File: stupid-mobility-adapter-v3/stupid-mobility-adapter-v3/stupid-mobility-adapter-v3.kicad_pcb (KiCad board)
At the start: 2 copper layers, 94.9 x 93.5 mm, 35 parts, among them J1 BTS7968-0, J2 Act0-FB, J3 BTS7968-1, J4 Act1-FB, J5 ESTOP_INPUT, J6 UART, J7 Relays, J8 I2C, J9 BATT_MON_SELECT, Q1 2N3904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

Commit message: Added buzzer and servo input to v3 pcb
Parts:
- added BZ1: Buzzer, stuipid-electronics-components:Buzzer_ABT-460-RC, F.Cu at (225.6, 99.8)
- added J10: UART, Connector_PinHeader_2.54mm:PinHeader_1x02_P2.54mm_Vertical, F.Cu at (213.9, 92.7)
- added R14: 100, Resistor_THT:R_Axial_DIN0207_L6.3mm_D2.5mm_P7.62mm_Horizontal, F.Cu at (220.7, 97.5)
- moved J7 53.9 mm to (235.2, 90.7), turned to 0 degrees
- moved U3 12.1 mm to (249.5, 98.0)
- moved R3 11.7 mm to (172.7, 92.7), turned to 180 degrees
- moved J6 5.59 mm to (188.7, 96.0)
- moved J8 5.59 mm to (188.7, 88.4)
- moved U1 5.39 mm to (193.5, 84.1)
- moved R5 4.13 mm to (165.1, 89.4), turned to 0 degrees
- moved J9 1.26 mm to (165.1, 85.6)
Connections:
- U5 pad 30: unconnected-(U5-Pad30) -> /px_steer
- U5 pad 31: unconnected-(U5-Pad31) -> /px_throttle
- U5 pad 32: unconnected-(U5-Pad32) -> Net-(R14-Pad2)
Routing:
- net /px_steer: track 0.00 -> 24.5 mm
- net /px_throttle: track 0.00 -> 20.8 mm
- net Net-(J7-Pad3): track 17.7 -> 35.2 mm
- net Net-(R14-Pad2): track 0.00 -> 15.4 mm
- net /BDI: track 100.7 -> 114.6 mm
- net Net-(J7-Pad2): track 23.4 -> 35.7 mm
- net /KEY_SW: track 52.7 -> 63.8 mm
- net /REV: track 50.2 -> 56.2 mm
- net Net-(BZ1-Pad1): track 0.00 -> 5.80 mm
- net /RX: track 10.9 -> 16.5 mm
- net /TX: track 7.26 -> 13.0 mm
- net Net-(F1-Pad2): track 14.1 -> 19.2 mm
- net /SCL: track 27.7 -> 31.3 mm
- net /BATT_MON: track 67.7 -> 70.8 mm
- net Net-(R7-Pad1): track 30.9 -> 33.8 mm
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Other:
- board text added: "RX"
- board text added: "SCL"
- board text added: "SDA"
- board text added: "TX"
- board text added: "px4_steer"
- board text added: "px4_throttle"

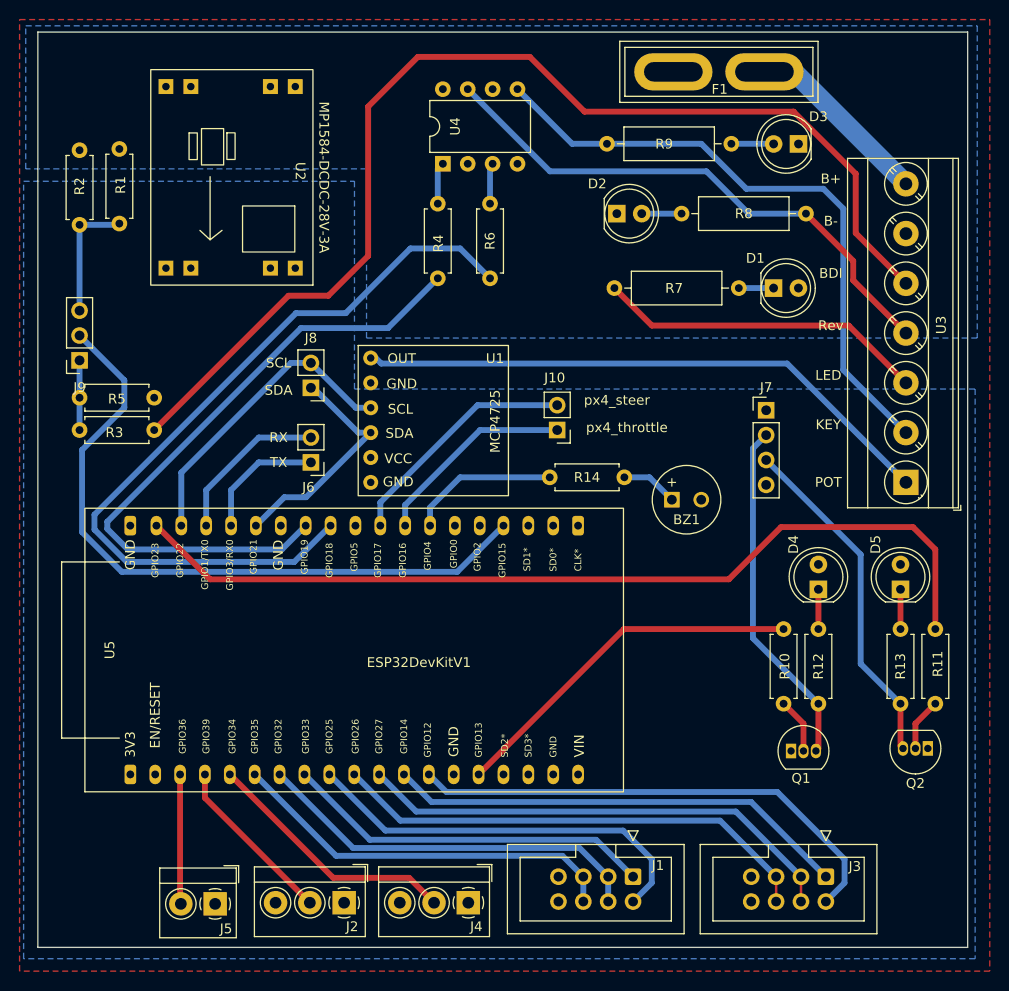
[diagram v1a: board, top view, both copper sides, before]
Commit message: Commit before doing first fork for new project
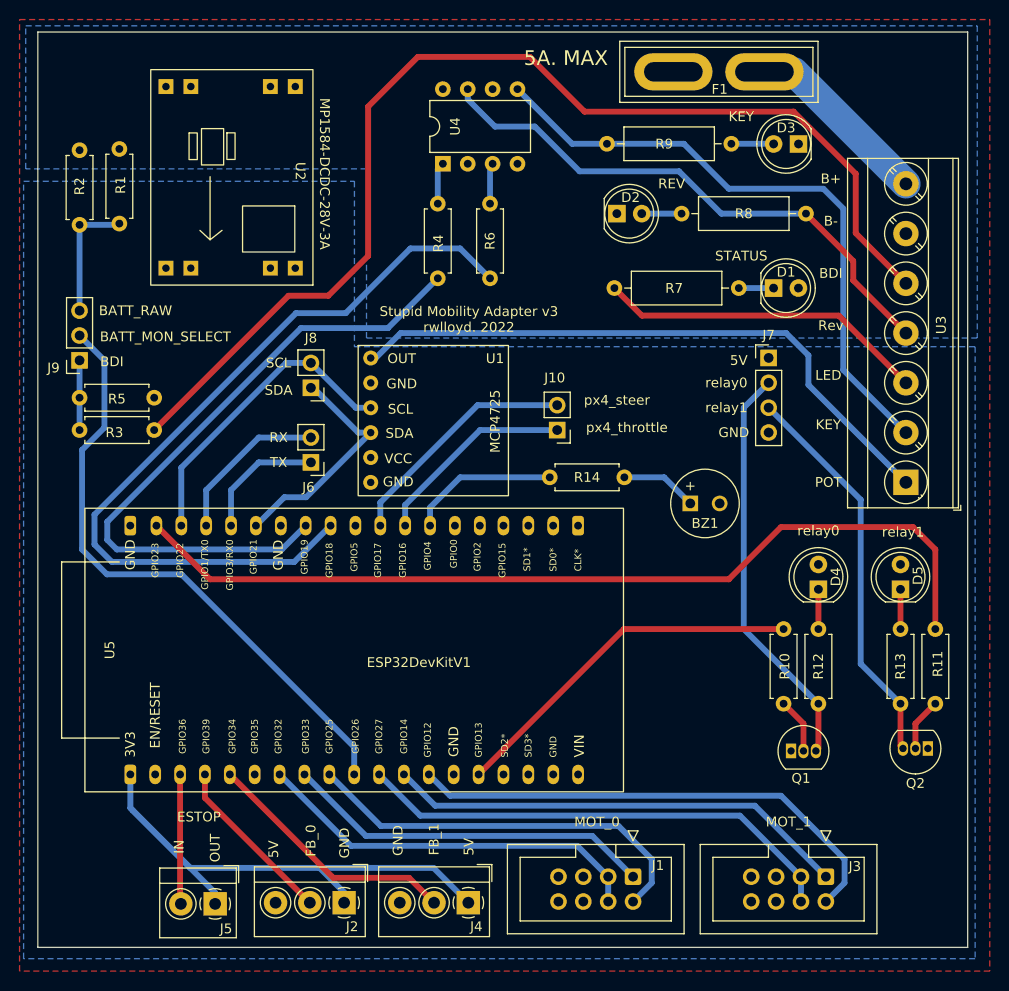
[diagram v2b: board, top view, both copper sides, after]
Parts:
- moved J7 5.35 mm to (235.5, 85.3)
- moved BZ1 1.92 mm to (227.5, 100.2)
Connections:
- J2 pad 1: VDD -> +3V3
- J3 pad 5: /BTS1_IS -> unconnected-(J3-Pad5)
- J3 pad 6: /BTS1_IS -> unconnected-(J3-Pad6)
- J4 pad 1: VDD -> +3V3
- J5 pad 1: VDD -> +3V3
- U5 pad 10: /BTS1_IS -> /BATT_MON
- U5 pad 19: unconnected-(U5-Pad19) -> +3V3
- U5 pad 35: /BATT_MON -> unconnected-(U5-Pad35)
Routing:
- net +3V3: track 0.00 -> 59.6 mm
- net /BTS1_IS: track 49.9 -> 0.00 mm
- net /BTS0_IS: track 40.4 -> 0.00 mm
- net /BATT_MON: track 70.8 -> 62.8 mm
- net Net-(J7-Pad2): track 35.7 -> 41.9 mm
- net Net-(J7-Pad3): track 35.2 -> 40.5 mm
- net /VOUT: track 59.9 -> 63.8 mm
- net Net-(BZ1-Pad1): track 5.80 -> 7.84 mm
- net /MOB_EN: track 81.4 -> 82.3 mm
- net /MOB_DIR: track 66.9 -> 67.6 mm
- net /REV: track 56.2 -> 56.8 mm
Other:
- board text added: "5A. MAX"
- board text added: "5V"
- board text added: "BATT_RAW"
- board text added: "ESTOP"
- board text added: "FB_0"
- board text added: "FB_1"
- board text added: "GND"
- board text added: "IN"
- board text added: "MOT_0"
- board text added: "MOT_1"
- board text added: "OUT"
- board text added: "REV"
- board text added: "STATUS"
- board text added: "Stupid Mobility Adapter v3 rwlloyd. 2022"
- board text added: "relay0"
- board text added: "relay1"

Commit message: build and setup board for v4.1/4.1
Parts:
- added 3.2: MountingHole_3.2mm_M3_DIN965_Pad, MountingHole:MountingHole_3.2mm_M3_DIN965_Pad, F.Cu at (251.7, 141.7)
- added 3.2: MountingHole_3.2mm_M3_DIN965_Pad, MountingHole:MountingHole_3.2mm_M3_DIN965_Pad, F.Cu at (164.5, 55.8)
- added 3.2: MountingHole_3.2mm_M3_DIN965_Pad, MountingHole:MountingHole_3.2mm_M3_DIN965_Pad, F.Cu at (164.6, 141.6)
- added 3.2: MountingHole_3.2mm_M3_DIN965_Pad, MountingHole:MountingHole_3.2mm_M3_DIN965_Pad, F.Cu at (252.0, 55.8)
- J9: footprint Connector_PinSocket_2.54mm:PinSocket_1x03_P2.54mm_Vertical -> Connector_PinHeader_2.54mm:PinHeader_1x03_P2.54mm_Vertical
- moved R14 10.5 mm to (226.2, 106.6), turned to -90 degrees
- moved BZ1 0.90 mm to (227.3, 101.1), turned to 90 degrees
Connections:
- J1 pad 5: /BTS0_IS -> unconnected-(J1-Pad5)
- J1 pad 6: /BTS0_IS -> unconnected-(J1-Pad6)
- R14 pad 2: Net-(R14-Pad2) -> /Buzz
- U5 pad 14: /BTS0_IS -> /Buzz
- U5 pad 32: Net-(R14-Pad2) -> /px_mode
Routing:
- net /Buzz: track 0.00 -> 48.9 mm
- net Net-(R14-Pad2): track 15.4 -> 0.00 mm
- net /relay1: track 93.1 -> 95.2 mm
- net Net-(BZ1-Pad1): track 7.84 -> 5.93 mm
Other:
- board text added: "Mobility Adapter v3 rwlloyd. 2022"
- board text added: "srv_steer"
- board text added: "srv_throttle"
- board text removed: "Stupid Mobility Adapter v3 rwlloyd. 2022"
- board text removed: "px4_steer"
- board text removed: "px4_throttle"
